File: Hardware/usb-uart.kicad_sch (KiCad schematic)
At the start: 9 parts, among them J5 USB_C_Receptacle_USB2.0

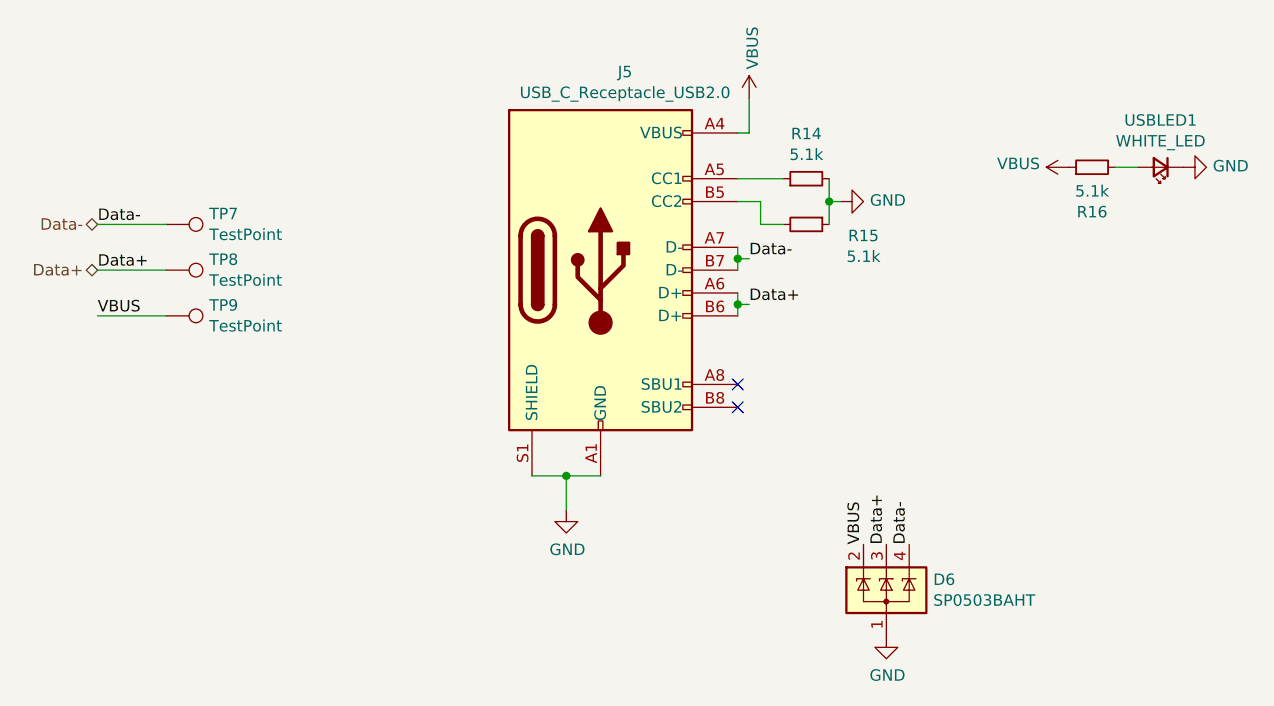
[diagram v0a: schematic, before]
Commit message: Updated Baseboard design but with power supply problems
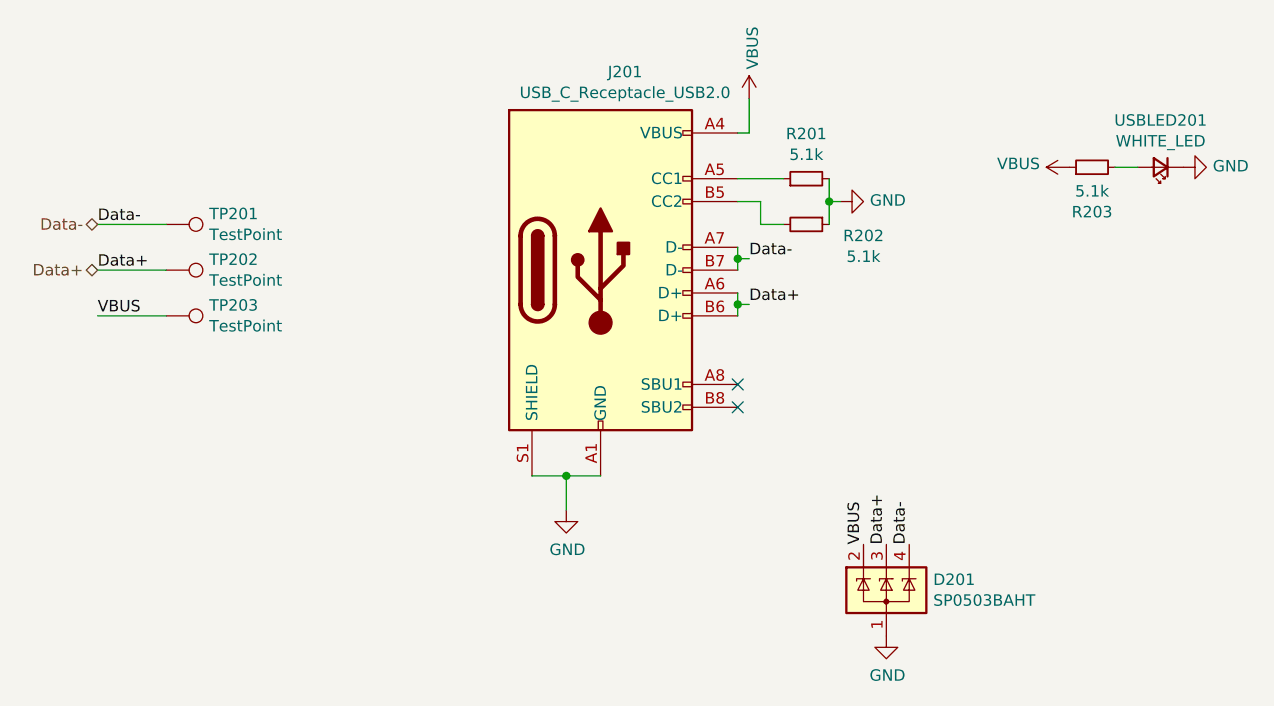
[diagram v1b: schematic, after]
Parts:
- renumbered D6 to D201, J5 to J201, R14 to R201, R15 to R202, R16 to R203, TP7 to TP201, TP8 to TP202, TP9 to TP203, USBLED1 to USBLED201
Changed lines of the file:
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@@
 (kicad_sch
-	(version 20231120)
+	(version 20250114)
 	(generator "eeschema")
-	(generator_version "8.0")
+	(generator_version "9.0")
 	(paper "A4")
 	(junction
@@
 		(on_board yes)
 		(dnp no)
-		(property "Reference" "#PWR038"
+		(property "Reference" "#PWR0203"
 			(at 133.35 96.52 0)
 			(effects
@@
 			(project "PickleRick"
 				(path "/e63e39d7-6ac0-4ffd-8aa3-1841a4541b55/dd5f5a5e-a654-455b-bff7-78de55e53413"
-					(reference "#PWR038")
+					(reference "#PWR0203")
 					(unit 1)
 				)
@@
 		(on_board yes)
 		(dnp no)
-		(property "Reference" "R15"
+		(property "Reference" "R202"
 			(at 129.54 100.33 90)
 			(effects
@@
 			(project "PickleRick"
 				(path "/e63e39d7-6ac0-4ffd-8aa3-1841a4541b55/dd5f5a5e-a654-455b-bff7-78de55e53413"
-					(reference "R15")
+					(reference "R202")
 					(unit 1)
 				)
@@
 		(on_board yes)
 		(dnp no)
-		(property "Reference" "R14"
+		(property "Reference" "R201"
 			(at 123.19 89.0016 90)
 			(effects
@@
 			(project "PickleRick"
 				(path "/e63e39d7-6ac0-4ffd-8aa3-1841a4541b55/dd5f5a5e-a654-455b-bff7-78de55e53413"
-					(reference "R14")
+					(reference "R201")
 					(unit 1)
 				)
@@
 		(on_board yes)
 		(dnp no)
-		(property "Reference" "#PWR036"
+		(property "Reference" "#PWR0201"
 			(at 96.52 137.16 0)
 			(effects
@@
 			(project "PickleRick"
 				(path "/e63e39d7-6ac0-4ffd-8aa3-1841a4541b55/dd5f5a5e-a654-455b-bff7-78de55e53413"
-					(reference "#PWR036")
+					(reference "#PWR0201")
 					(unit 1)
 				)
@@
 		(on_board yes)
 		(dnp no)
-		(property "Reference" "J5"
+		(property "Reference" "J201"
 			(at 103.0478 82.1182 0)
 			(effects
@@
 			(project "PickleRick"
 				(path "/e63e39d7-6ac0-4ffd-8aa3-1841a4541b55/dd5f5a5e-a654-455b-bff7-78de55e53413"
-					(reference "J5")
+					(reference "J201")
 					(unit 1)
 				)
@@
 		(on_board yes)
 		(dnp no)
-		(property "Reference" "#PWR039"
+		(property "Reference" "#PWR0204"
 			(at 132.08 151.13 0)
 			(effects
@@
 			(project "PickleRick"
 				(path "/e63e39d7-6ac0-4ffd-8aa3-1841a4541b55/dd5f5a5e-a654-455b-bff7-78de55e53413"
-					(reference "#PWR039")
+					(reference "#PWR0204")
 					(unit 1)
 				)
@@
 		(on_board yes)
 		(dnp no)
-		(property "Reference" "D6"
+		(property "Reference" "D201"
 			(at 137.287 138.5316 0)
 			(effects
@@
 			(project "PickleRick"
 				(path "/e63e39d7-6ac0-4ffd-8aa3-1841a4541b55/dd5f5a5e-a654-455b-bff7-78de55e53413"
-					(reference "D6")
+					(reference "D201")
 					(unit 1)
 				)
@@
 		(on_board yes)
 		(dnp no)
-		(property "Reference" "#PWR037"
+		(property "Reference" "#PWR0202"
 			(at 116.84 88.9 0)
 			(effects
@@
 			(project "PickleRick"
 				(path "/e63e39d7-6ac0-4ffd-8aa3-1841a4541b55/dd5f5a5e-a654-455b-bff7-78de55e53413"
-					(reference "#PWR037")
+					(reference "#PWR0202")
 					(unit 1)
 				)
@@
 		(on_board yes)
 		(dnp no)
-		(property "Reference" "TP7"
+		(property "Reference" "TP201"
 			(at 56.8452 97.8916 90)
 			(effects
@@
 			(project "PickleRick"
 				(path "/e63e39d7-6ac0-4ffd-8aa3-1841a4541b55/dd5f5a5e-a654-455b-bff7-78de55e53413"
-					(reference "TP7")
+					(reference "TP201")
 					(unit 1)
 				)
@@
 		(on_board yes)
 		(dnp no)
-		(property "Reference" "TP8"
+		(property "Reference" "TP202"
 			(at 56.8452 102.9716 90)
 			(effects
@@
 			(project "PickleRick"
 				(path "/e63e39d7-6ac0-4ffd-8aa3-1841a4541b55/dd5f5a5e-a654-455b-bff7-78de55e53413"
-					(reference "TP8")
+					(reference "TP202")
 					(unit 1)
 				)
@@
 		(on_board yes)
 		(dnp no)
-		(property "Reference" "TP9"
+		(property "Reference" "TP203"
 			(at 56.8452 108.0516 90)
 			(effects
@@
 			(project "PickleRick"
 				(path "/e63e39d7-6ac0-4ffd-8aa3-1841a4541b55/dd5f5a5e-a654-455b-bff7-78de55e53413"
-					(reference "TP9")
+					(reference "TP203")
 					(unit 1)
 				)
@@
 		(on_board yes)
 		(dnp no)
-		(property "Reference" "USBLED1"
+		(property "Reference" "USBLED201"
 			(at 162.56 87.503 0)
 			(effects
@@
 			(project "PickleRick"
 				(path "/e63e39d7-6ac0-4ffd-8aa3-1841a4541b55/dd5f5a5e-a654-455b-bff7-78de55e53413"
-					(reference "USBLED1")
+					(reference "USBLED201")
 					(unit 1)
 				)
@@
 		(on_board yes)
 		(dnp no)
-		(property "Reference" "R16"
+		(property "Reference" "R203"
 			(at 154.94 97.6884 90)
 			(effects
@@
 			(project "PickleRick"
 				(path "/e63e39d7-6ac0-4ffd-8aa3-1841a4541b55/dd5f5a5e-a654-455b-bff7-78de55e53413"
-					(reference "R16")
+					(reference "R203")
 					(unit 1)
 				)
@@
 		(on_board yes)
 		(dnp no)
-		(property "Reference" "#PWR041"
+		(property "Reference" "#PWR0206"
 			(at 171.45 92.71 0)
 			(effects
@@
 			(project "PickleRick"
 				(path "/e63e39d7-6ac0-4ffd-8aa3-1841a4541b55/dd5f5a5e-a654-455b-bff7-78de55e53413"
-					(reference "#PWR041")
+					(reference "#PWR0206")
 					(unit 1)
 				)
@@
 		(on_board yes)
 		(dnp no)
-		(property "Reference" "#PWR040"
+		(property "Reference" "#PWR0205"
 			(at 156.21 92.71 0)
 			(effects
@@
 			(project "PickleRick"
 				(path "/e63e39d7-6ac0-4ffd-8aa3-1841a4541b55/dd5f5a5e-a654-455b-bff7-78de55e53413"
-					(reference "#PWR040")
-					(unit 1)
-				)
+					(reference "#PWR0205")
+					(unit 1)
+				)
